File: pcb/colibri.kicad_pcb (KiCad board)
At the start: 2 copper layers, 169 x 202.2 mm, 208 parts

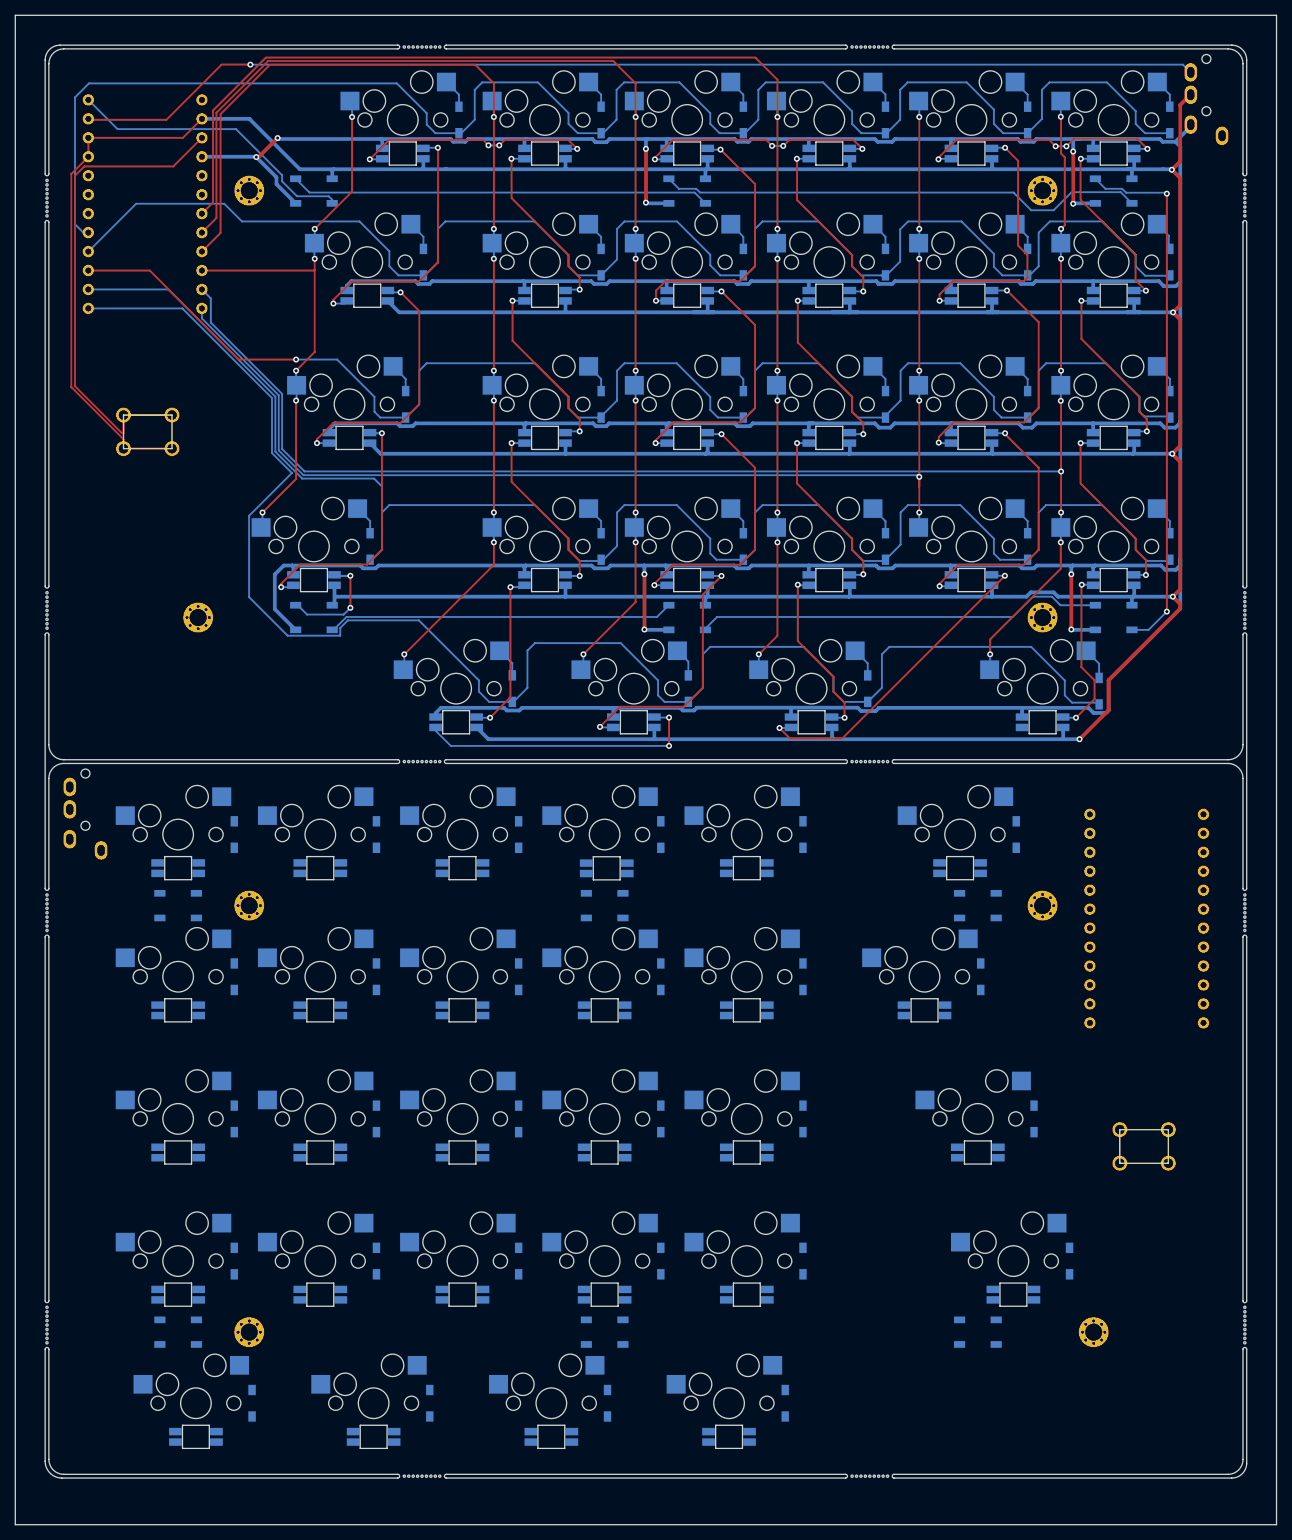
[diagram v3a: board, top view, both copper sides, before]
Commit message: rows connected on the right side
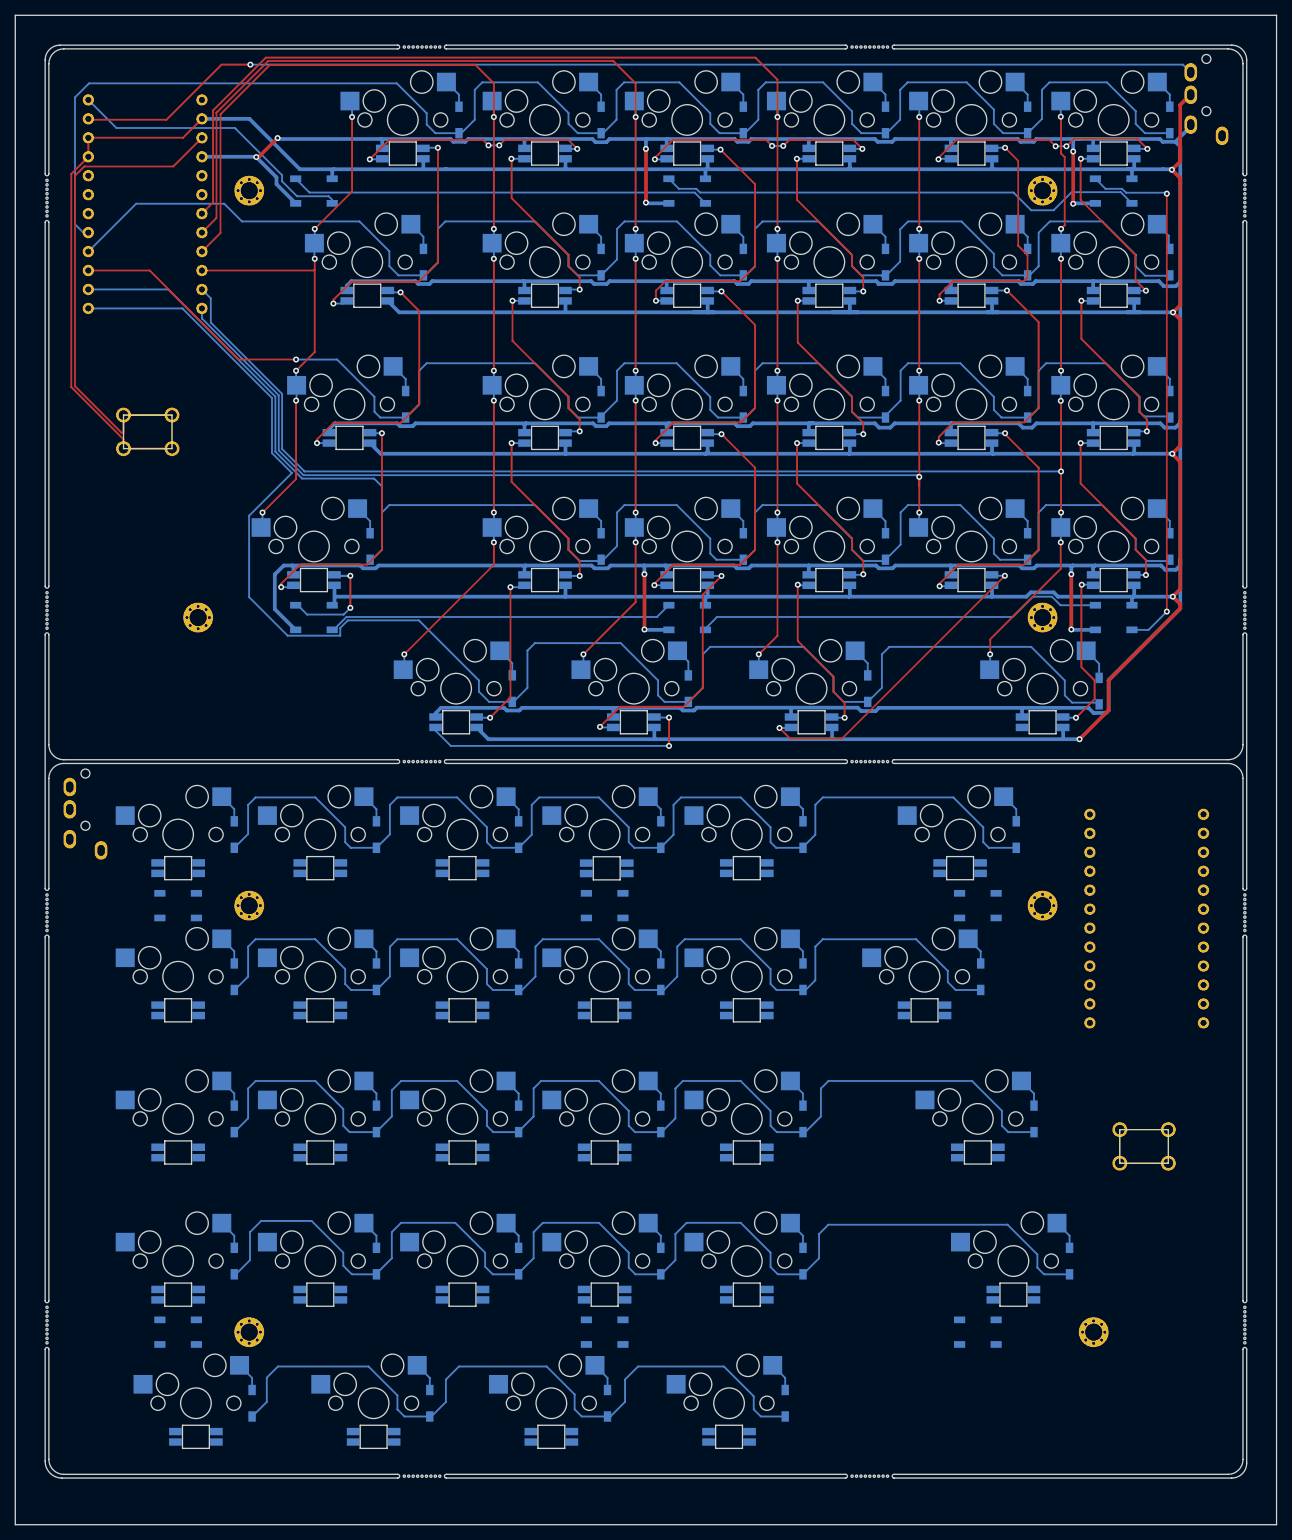
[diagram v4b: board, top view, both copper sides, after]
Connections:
- net rGND renamed GND2
- net rVCC renamed VDD
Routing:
- net rrow3: track 0.00 -> 156.3 mm
- net rrow2: track 0.00 -> 152.7 mm
- net rrow0: track 0.00 -> 150.3 mm
- net rrow1: track 0.00 -> 145.8 mm
- net rrow4: track 0.00 -> 96.8 mm
- net Net-(rd-7-Pad2): track 0.00 -> 4.00 mm
- net Net-(rd-28-Pad2): track 0.00 -> 4.00 mm
- net Net-(rd-20-Pad2): track 0.00 -> 4.00 mm
- net Net-(rd-13-Pad2): track 0.00 -> 4.00 mm
- net Net-(rd-9-Pad2): track 0.00 -> 4.00 mm
- net Net-(rd-8-Pad2): track 0.00 -> 4.00 mm
- net Net-(rd-3-Pad2): track 0.00 -> 4.00 mm
- net Net-(rd-21-Pad2): track 0.00 -> 4.00 mm
- net Net-(rd-2-Pad2): track 0.00 -> 4.00 mm
- net Net-(rd-6-Pad2): track 0.00 -> 4.00 mm
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
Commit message: right side done
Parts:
- turned ru-1 to 0 degrees
- turned ru-2 to 0 degrees
- turned ru-3 to 0 degrees
- turned ru-4 to 0 degrees
- turned ru-5 to 0 degrees
- turned ru-6 to 0 degrees
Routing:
- net VDD: track 0.00 -> 788.5 mm, vias 0 -> 10
- net GND2: track 0.00 -> 787.1 mm, vias 0 -> 5
- net rcol5: track 0.00 -> 256.7 mm, vias 0 -> 9
- net rcol4: track 0.00 -> 248.1 mm, vias 0 -> 9
- net rcol3: track 0.00 -> 240.4 mm, vias 0 -> 9
- net rcol2: track 0.00 -> 206.3 mm, vias 0 -> 9
- net rcol1: track 0.00 -> 154.5 mm, vias 0 -> 7
- net rdata: track 0.00 -> 139.9 mm
- net rcol0: track 0.00 -> 108.6 mm, vias 0 -> 7
- net rrow4: track 96.8 -> 179.1 mm
- net Net-(ru-3-Pad2): track 0.00 -> 72.6 mm, vias 0 -> 2
- net Net-(ru-5-Pad4): track 0.00 -> 65.7 mm
- net Net-(ru-4-Pad4): track 0.00 -> 56.3 mm
- net Net-(ru-2-Pad2): track 0.00 -> 54.0 mm
- net rreset: track 0.00 -> 49.0 mm
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
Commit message: added colibri logo
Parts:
- added G***: LOGO, kbd:colibri-logo, F.Cu at (165.0, 218.9)
- added G***: LOGO, kbd:colibri-logo, F.Cu at (45.0, 123.2)
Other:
- board text added: "colibri keyboard by @tangzero version 1.0"
